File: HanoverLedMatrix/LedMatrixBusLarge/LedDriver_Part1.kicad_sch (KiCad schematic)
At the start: 200 parts

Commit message: feat: Updated the symbol of 74HC373D
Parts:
- D? (x160): value (none) -> LED_Small
- R? (x20): value (none) -> 3K
- U? (x20): value (none) -> MBI5167G

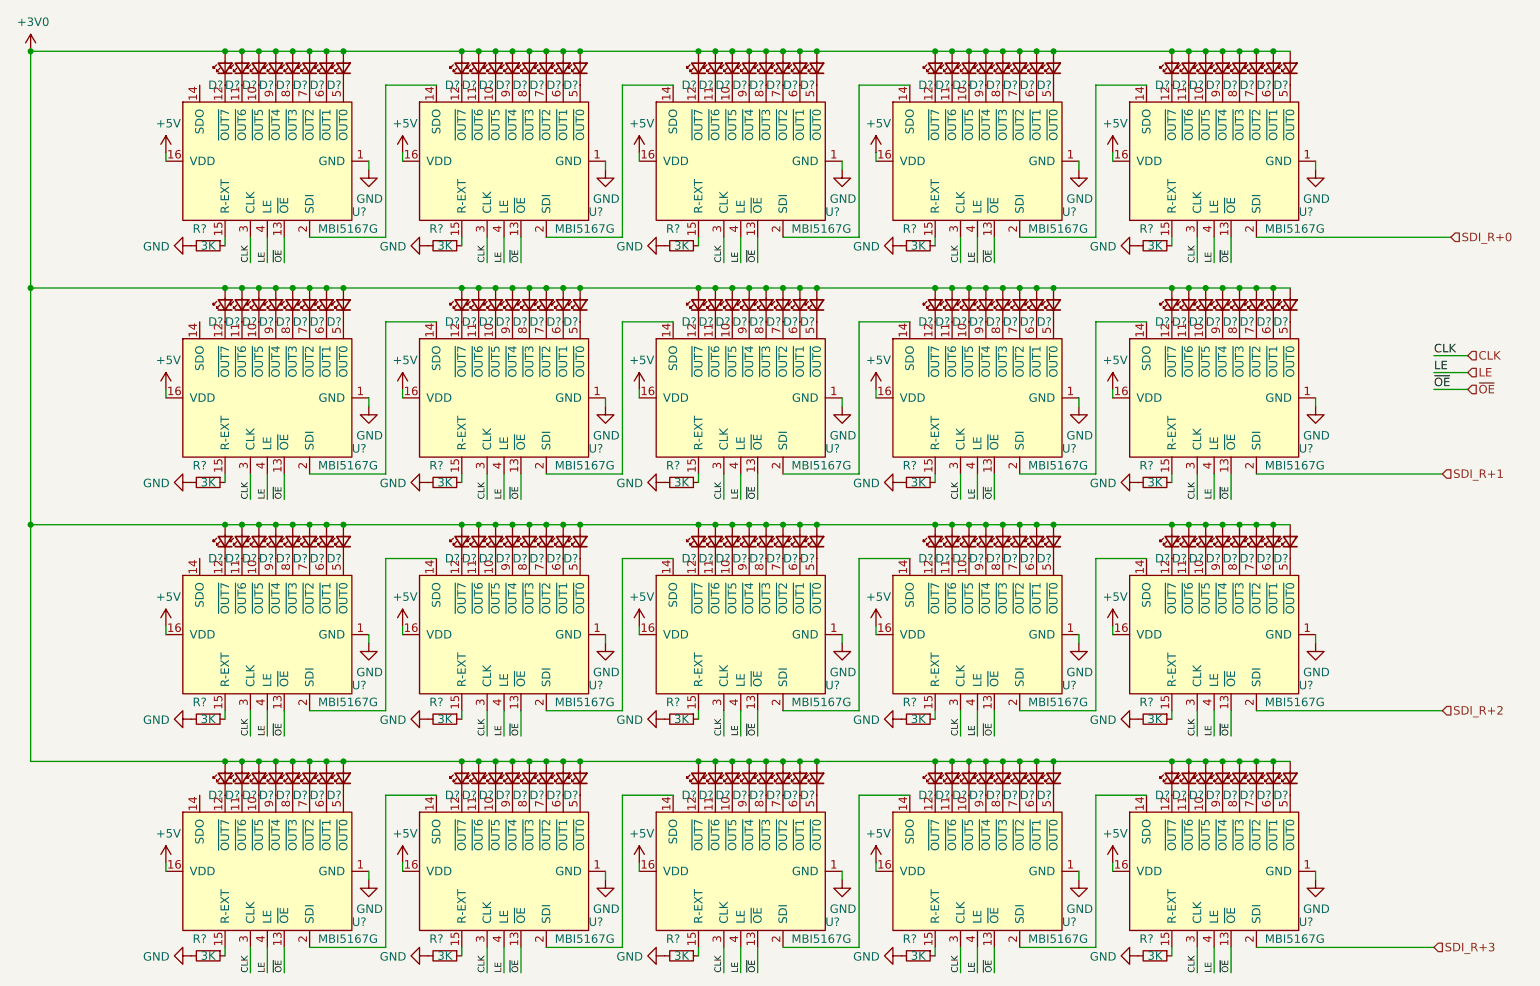
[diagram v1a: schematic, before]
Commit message: feat: organised the schematic into blocks and updated the readme
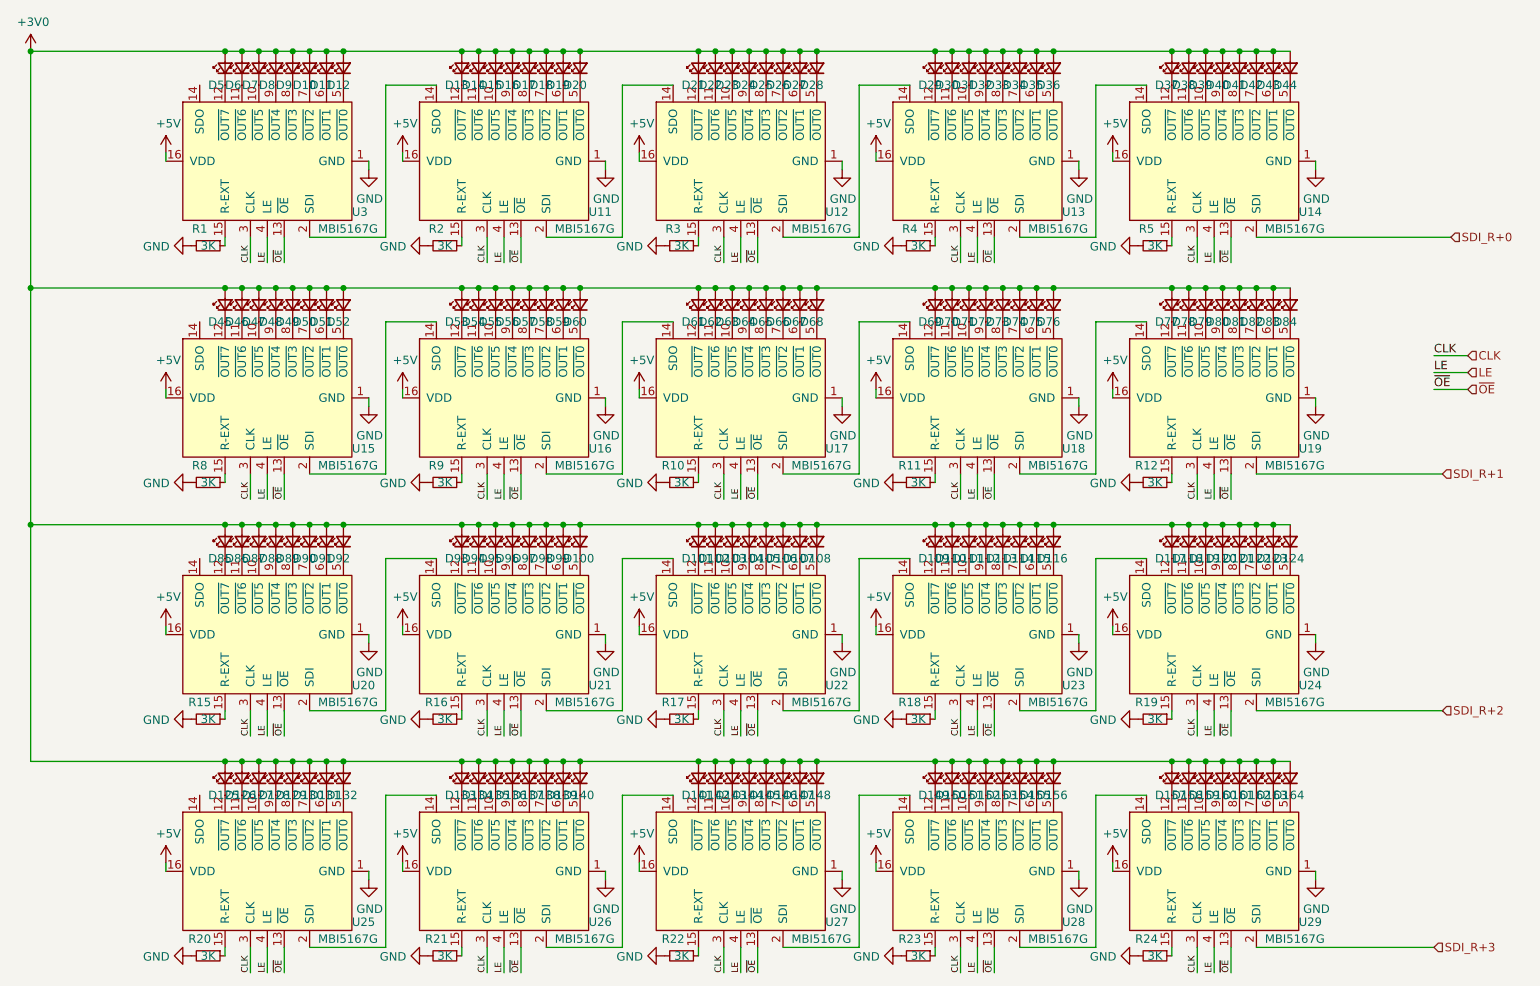
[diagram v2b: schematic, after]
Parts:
- gave numbers to parts that had none: 200
